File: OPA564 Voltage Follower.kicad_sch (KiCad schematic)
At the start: 13 parts, among them IC1 OPA564AIDWD, IC2 OPA564AIDWD, J1 Conn_Coaxial, J2 Conn_Coaxial

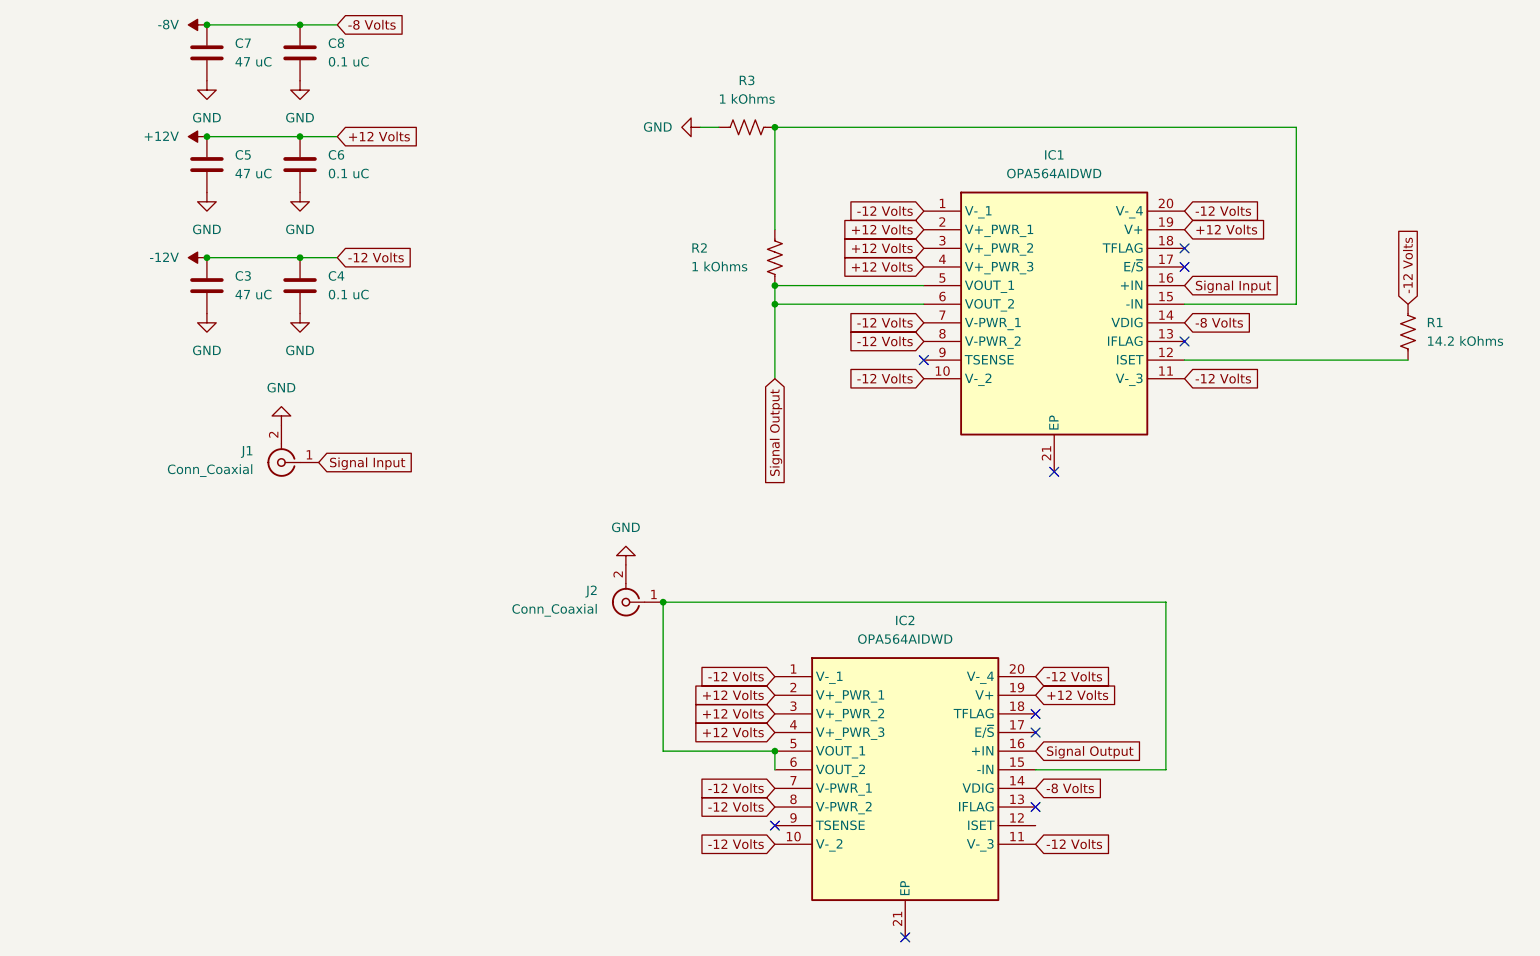
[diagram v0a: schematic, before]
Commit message: A lot of silkscreen clearance issues :( but got the voltage follower done
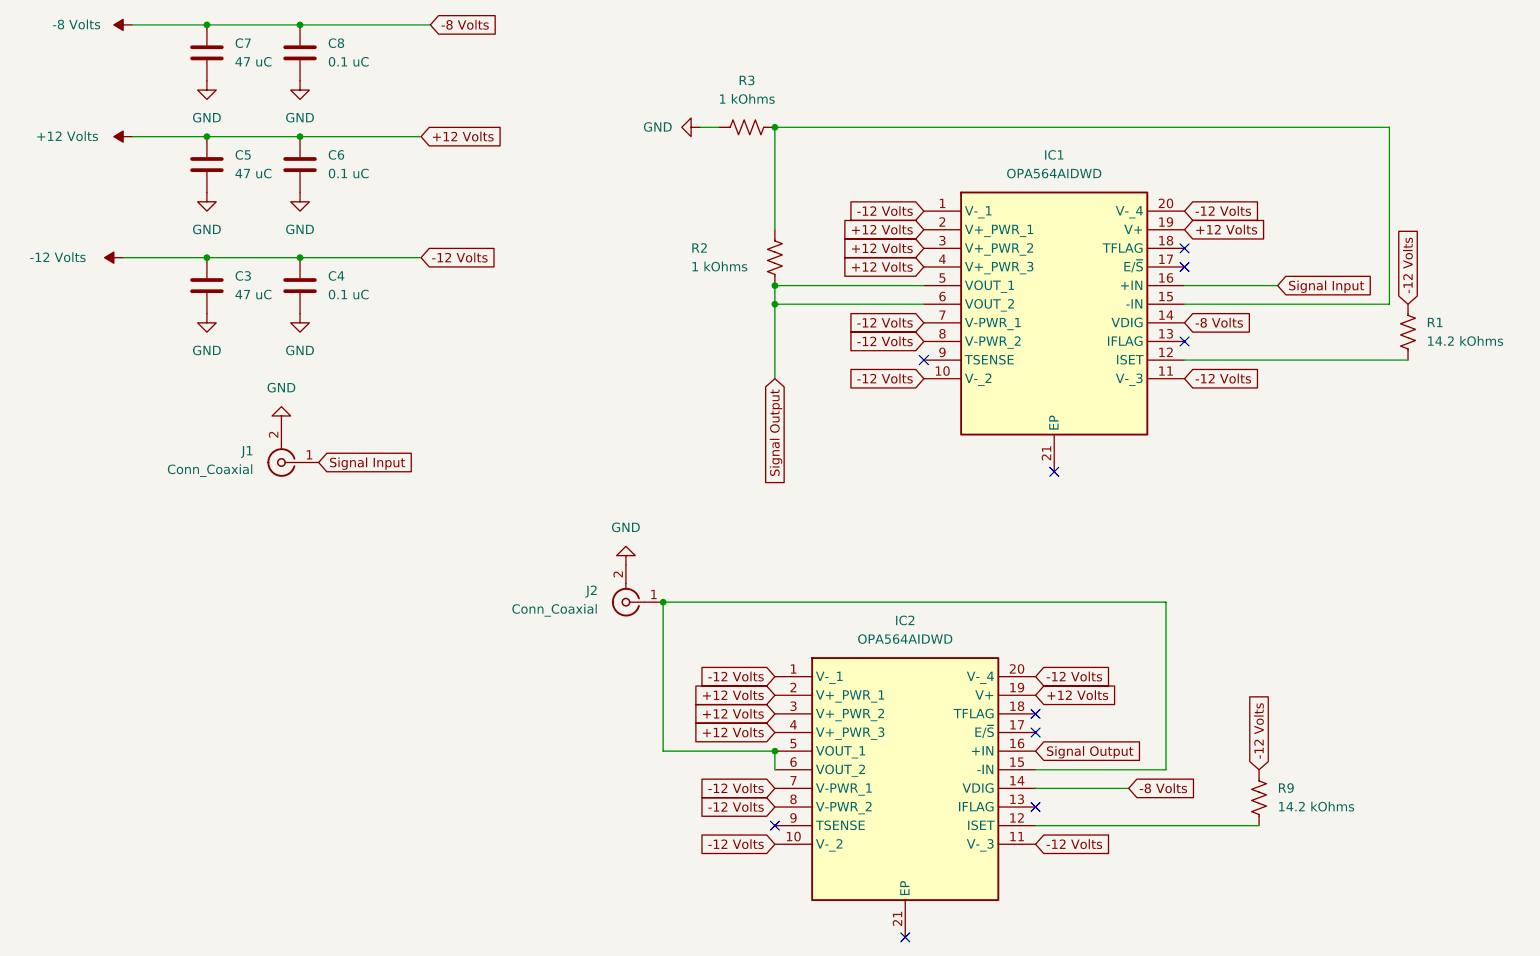
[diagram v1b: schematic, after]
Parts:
- added R9: 14.2 kOhms, Resistor_SMD:R_0805_2012Metric_Pad1.20x1.40mm_HandSolder, symbol Device:R_US
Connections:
- net at IC2.12 (ISET): now also R9.2
- net +12V renamed +12 Volts
- net -12V renamed -12 Volts
- net -12 Volts: now also R9.1
- net -8V renamed -8 Volts
